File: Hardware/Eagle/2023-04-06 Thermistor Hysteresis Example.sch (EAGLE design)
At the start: 7 parts, among them U1 LMV339

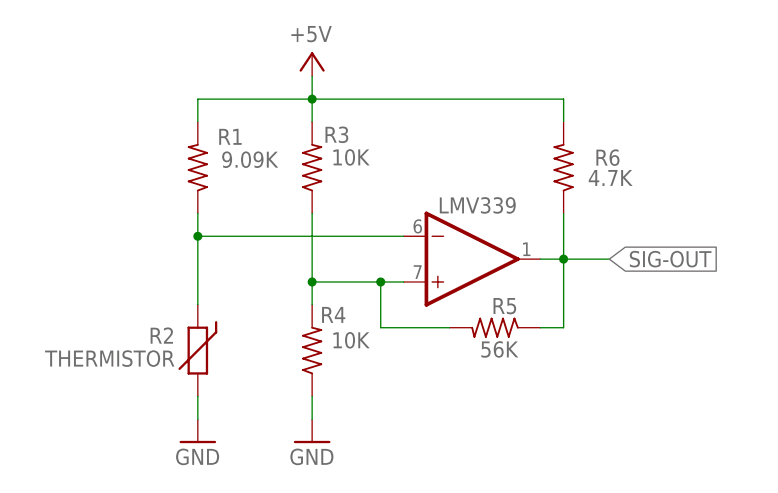
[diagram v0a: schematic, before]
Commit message: LN2 autofill update
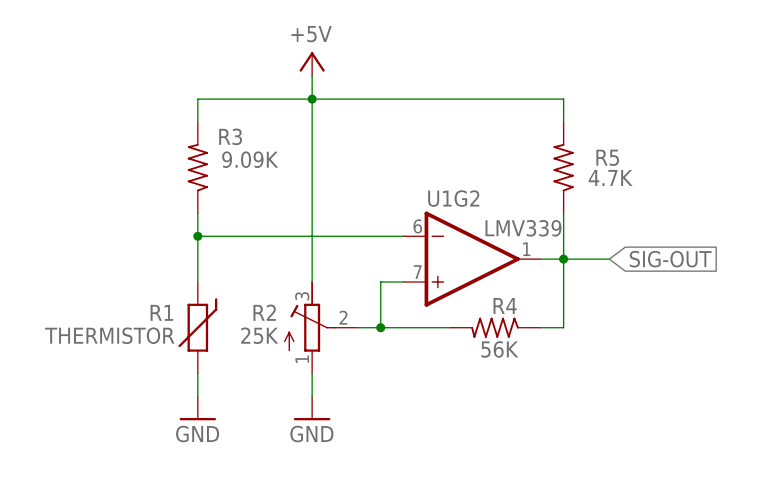
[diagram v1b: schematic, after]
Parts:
- removed R6: 4.7K, AUmlib:R-US_R0805
- R1: value 9.09K -> THERMISTOR; device AUmlib:R-US_R0805 -> varistor:THERMISTOR-7,5
- R2: value THERMISTOR -> 25K; device varistor:THERMISTOR-7,5 -> AUmlib:R-TRIMM3296Y
- R3: value 10K -> 9.09K
- R4: value 10K -> 56K
- R5: value 56K -> 4.7K
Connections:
- net +5V: now also R2.E, R5.2; no longer R1.2, R6.2
- net GND: now also R1.2, R2.A; no longer R2.2, R4.1
- net SIG-OUT: now also R4.1; no longer R6.1
- net THER3-IN: now also R3.1; no longer R2.1
- net TRIM3: now also R2.S; no longer R3.1, R5.2
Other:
- moved on the sheet: R3, R4, R5
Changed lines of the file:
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@@
 <?xml version="1.0" encoding="utf-8"?>
 <!DOCTYPE eagle SYSTEM "eagle.dtd">
-<eagle version="9.6.2">
+<eagle version="9.5.2">
 <drawing>
 <settings>
@@
 <setting verticaltext="up"/>
 </settings>
-<grid distance="0.05" unitdist="inch" unit="inch" style="lines" multiple="1" display="yes" altdistance="0.01" altunitdist="inch" altunit="inch"/>
+<grid distance="0.1" unitdist="inch" unit="inch" style="lines" multiple="1" display="yes" altdistance="0.01" altunitdist="inch" altunit="inch"/>
 <layers>
 <layer number="1" name="Top" color="4" fill="1" visible="no" active="no"/>
@@
 </classes>
 <parts>
-<part name="R6" library="AUmlib" library_urn="urn:adsk.eagle:library:9166017" deviceset="R-US_" device="R0805" package3d_urn="urn:adsk.eagle:package:4021199/4" value="4.7K"/>
+<part name="R5" library="AUmlib" library_urn="urn:adsk.eagle:library:9166017" deviceset="R-US_" device="R0805" package3d_urn="urn:adsk.eagle:package:4021199/1" value="4.7K"/>
 <part name="P+3" library="AUmlib" library_urn="urn:adsk.eagle:library:9166017" deviceset="+5V" device=""/>
-<part name="R5" library="AUmlib" library_urn="urn:adsk.eagle:library:9166017" deviceset="R-US_" device="R0805" package3d_urn="urn:adsk.eagle:package:4021199/4" value="56K"/>
-<part name="R1" library="AUmlib" library_urn="urn:adsk.eagle:library:9166017" deviceset="R-US_" device="R0805" package3d_urn="urn:adsk.eagle:package:4021199/4" value="9.09K"/>
+<part name="R4" library="AUmlib" library_urn="urn:adsk.eagle:library:9166017" deviceset="R-US_" device="R0805" package3d_urn="urn:adsk.eagle:package:4021199/1" value="56K"/>
+<part name="R3" library="AUmlib" library_urn="urn:adsk.eagle:library:9166017" deviceset="R-US_" device="R0805" package3d_urn="urn:adsk.eagle:package:4021199/1" value="9.09K"/>
+<part name="R2" library="AUmlib" library_urn="urn:adsk.eagle:library:9166017" deviceset="R-TRIMM" device="3296Y" package3d_urn="urn:adsk.eagle:package:16459115/2" value="25K"/>
 <part name="U1" library="AUmlib" library_urn="urn:adsk.eagle:library:9166017" deviceset="LM339" device="SOIC-14" package3d_urn="urn:adsk.eagle:package:3812082/2" value="LMV339"/>
-<part name="R2" library="varistor" library_urn="urn:adsk.eagle:library:410" deviceset="THERMISTOR" device="-7,5" package3d_urn="urn:adsk.eagle:package:30593/1" value="THERMISTOR"/>
+<part name="R1" library="varistor" library_urn="urn:adsk.eagle:library:410" deviceset="THERMISTOR" device="-7,5" package3d_urn="urn:adsk.eagle:package:30593/1" value="THERMISTOR"/>
 <part name="GND1" library="AUmlib" library_urn="urn:adsk.eagle:library:9166017" deviceset="GND" device=""/>
 <part name="GND2" library="AUmlib" library_urn="urn:adsk.eagle:library:9166017" deviceset="GND" device=""/>
-<part name="R3" library="AUmlib" library_urn="urn:adsk.eagle:library:9166017" deviceset="R-US_" device="R0805" package3d_urn="urn:adsk.eagle:package:4021199/4" value="10K"/>
-<part name="R4" library="AUmlib" library_urn="urn:adsk.eagle:library:9166017" deviceset="R-US_" device="R0805" package3d_urn="urn:adsk.eagle:package:4021199/4" value="10K"/>
 </parts>
 <sheets>
@@
 </plain>
 <instances>
-<instance part="R6" gate="G$1" x="50.8" y="35.56" smashed="yes" rot="MR90">
+<instance part="R5" gate="G$1" x="50.8" y="35.56" smashed="yes" rot="MR90">
 <attribute name="NAME" x="57.15" y="35.7886" size="1.778" layer="95" rot="MR0"/>
 <attribute name="VALUE" x="58.42" y="33.528" size="1.778" layer="96" rot="MR0"/>
@@
 <attribute name="VALUE" x="20.32" y="49.53" size="1.778" layer="96" rot="MR0" align="bottom-right"/>
 </instance>
-<instance part="R5" gate="G$1" x="43.18" y="17.78" smashed="yes" rot="MR0">
+<instance part="R4" gate="G$1" x="43.18" y="17.78" smashed="yes" rot="MR0">
 <attribute name="NAME" x="45.72" y="19.304" size="1.778" layer="95" rot="MR0"/>
 <attribute name="VALUE" x="45.72" y="14.478" size="1.778" layer="96" rot="MR0"/>
 </instance>
-<instance part="R1" gate="G$1" x="10.16" y="35.56" smashed="yes" rot="MR90">
+<instance part="R3" gate="G$1" x="10.16" y="35.56" smashed="yes" rot="MR90">
 <attribute name="NAME" x="15.24" y="38.1" size="1.778" layer="95" rot="MR0"/>
 <attribute name="VALUE" x="19.05" y="35.56" size="1.778" layer="96" rot="MR0"/>
 </instance>
+<instance part="R2" gate="G$1" x="22.86" y="17.78" smashed="yes">
+<attribute name="NAME" x="19.05" y="20.32" size="1.778" layer="95" rot="R180"/>
+<attribute name="VALUE" x="19.05" y="17.78" size="1.778" layer="96" rot="R180"/>
+</instance>
 <instance part="U1" gate="G2" x="40.64" y="25.4" smashed="yes">
-<attribute name="VALUE" x="36.83" y="30.48" size="1.778" layer="95"/>
-</instance>
-<instance part="R2" gate="G$1" x="10.16" y="15.24" smashed="yes" rot="R90">
-<attribute name="NAME" x="7.62" y="17.78" size="1.778" layer="95" rot="R180"/>
-<attribute name="VALUE" x="7.62" y="15.24" size="1.778" layer="96" rot="R180"/>
-</instance>
-<instance part="GND1" gate="1" x="22.86" y="5.08" smashed="yes">
-<attribute name="VALUE" x="20.32" y="2.54" size="1.778" layer="96"/>
-</instance>
-<instance part="GND2" gate="1" x="10.16" y="5.08" smashed="yes">
-<attribute name="VALUE" x="7.62" y="2.54" size="1.778" layer="96"/>
-</instance>
-<instance part="R3" gate="G$1" x="22.86" y="35.56" smashed="yes" rot="R90">
-<attribute name="NAME" x="24.13" y="38.3286" size="1.778" layer="95"/>
-<attribute name="VALUE" x="29.21" y="37.592" size="1.778" layer="96" rot="R180"/>
-</instance>
-<instance part="R4" gate="G$1" x="22.86" y="15.24" smashed="yes" rot="R90">
-<attribute name="NAME" x="26.67" y="20.0914" size="1.778" layer="95" rot="R180"/>
-<attribute name="VALUE" x="29.21" y="17.272" size="1.778" layer="96" rot="R180"/>
+<attribute name="NAME" x="35.56" y="31.242" size="1.778" layer="95"/>
+<attribute name="VALUE" x="41.91" y="27.94" size="1.778" layer="95"/>
+</instance>
+<instance part="R1" gate="G$1" x="10.16" y="17.78" smashed="yes" rot="R90">
+<attribute name="NAME" x="7.62" y="20.32" size="1.778" layer="95" rot="R180"/>
+<attribute name="VALUE" x="7.62" y="17.78" size="1.778" layer="96" rot="R180"/>
+</instance>
+<instance part="GND1" gate="1" x="22.86" y="7.62" smashed="yes">
+<attribute name="VALUE" x="20.32" y="5.08" size="1.778" layer="96"/>
+</instance>
+<instance part="GND2" gate="1" x="10.16" y="7.62" smashed="yes">
+<attribute name="VALUE" x="7.62" y="5.08" size="1.778" layer="96"/>
 </instance>
 </instances>
@@
 <net name="SIG-OUT" class="0">
 <segment>
-<pinref part="R6" gate="G$1" pin="1"/>
+<pinref part="R5" gate="G$1" pin="1"/>
 <wire x1="50.8" y1="30.48" x2="50.8" y2="25.4" width="0.1524" layer="91"/>
-<pinref part="R5" gate="G$1" pin="1"/>
+<pinref part="R4" gate="G$1" pin="1"/>
 <wire x1="48.26" y1="17.78" x2="50.8" y2="17.78" width="0.1524" layer="91"/>
 <wire x1="50.8" y1="17.78" x2="50.8" y2="25.4" width="0.1524" layer="91"/>
@@
 <net name="TRIM3" class="0">
 <segment>
-<pinref part="R5" gate="G$1" pin="2"/>
+<pinref part="R4" gate="G$1" pin="2"/>
 <wire x1="38.1" y1="17.78" x2="30.48" y2="17.78" width="0.1524" layer="91"/>
 <wire x1="30.48" y1="17.78" x2="30.48" y2="22.86" width="0.1524" layer="91"/>
+<wire x1="30.48" y1="17.78" x2="27.94" y2="17.78" width="0.1524" layer="91"/>
+<junction x="30.48" y="17.78"/>
+<pinref part="R2" gate="G$1" pin="S"/>
 <pinref part="U1" gate="G2" pin="+IN"/>
 <wire x1="33.02" y1="22.86" x2="30.48" y2="22.86" width="0.1524" layer="91"/>
+</segment>
+</net>
+<net name="THER3-IN" class="0">
+<segment>
 <pinref part="R3" gate="G$1" pin="1"/>
-<pinref part="R4" gate="G$1" pin="2"/>
-<wire x1="22.86" y1="30.48" x2="22.86" y2="22.86" width="0.1524" layer="91"/>
-<wire x1="22.86" y1="22.86" x2="22.86" y2="20.32" width="0.1524" layer="91"/>
-<wire x1="22.86" y1="22.86" x2="30.48" y2="22.86" width="0.1524" layer="91"/>
-<junction x="22.86" y="22.86"/>
-<junction x="30.48" y="22.86"/>
-</segment>
-</net>
-<net name="THER3-IN" class="0">
-<segment>
 <pinref part="R1" gate="G$1" pin="1"/>
-<pinref part="R2" gate="G$1" pin="1"/>
-<wire x1="10.16" y1="20.32" x2="10.16" y2="27.94" width="0.1524" layer="91"/>
+<wire x1="10.16" y1="22.86" x2="10.16" y2="27.94" width="0.1524" layer="91"/>
 <pinref part="U1" gate="G2" pin="-IN"/>
 <wire x1="10.16" y1="27.94" x2="10.16" y2="30.48" width="0.1524" layer="91"/>
@@
 <net name="GND" class="0">
 <segment>
+<pinref part="R2" gate="G$1" pin="A"/>
 <pinref part="GND1" gate="1" pin="GND"/>
-<wire x1="22.86" y1="7.62" x2="22.86" y2="10.16" width="0.1524" layer="91"/>
-<pinref part="R4" gate="G$1" pin="1"/>
+<wire x1="22.86" y1="10.16" x2="22.86" y2="12.7" width="0.1524" layer="91"/>
 </segment>
 <segment>
 <pinref part="GND2" gate="1" pin="GND"/>
-<pinref part="R2" gate="G$1" pin="2"/>
-<wire x1="10.16" y1="7.62" x2="10.16" y2="10.16" width="0.1524" layer="91"/>
+<pinref part="R1" gate="G$1" pin="2"/>
+<wire x1="10.16" y1="10.16" x2="10.16" y2="12.7" width="0.1524" layer="91"/>
 </segment>
 </net>
 <net name="+5V" class="0">
 <segment>
-<pinref part="R6" gate="G$1" pin="2"/>
+<pinref part="R5" gate="G$1" pin="2"/>
 <wire x1="50.8" y1="40.64" x2="50.8" y2="43.18" width="0.1524" layer="91"/>
 <wire x1="50.8" y1="43.18" x2="22.86" y2="43.18" width="0.1524" layer="91"/>
 <wire x1="10.16" y1="43.18" x2="22.86" y2="43.18" width="0.1524" layer="91"/>
+<wire x1="22.86" y1="43.18" x2="22.86" y2="22.86" width="0.1524" layer="91"/>
+<pinref part="R2" gate="G$1" pin="E"/>
 <pinref part="P+3" gate="1" pin="+5V"/>
 <wire x1="22.86" y1="43.18" x2="22.86" y2="45.72" width="0.1524" layer="91"/>
 <junction x="22.86" y="43.18"/>
-<pinref part="R1" gate="G$1" pin="2"/>
+<pinref part="R3" gate="G$1" pin="2"/>
 <wire x1="10.16" y1="40.64" x2="10.16" y2="43.18" width="0.1524" layer="91"/>
-<pinref part="R3" gate="G$1" pin="2"/>
-<wire x1="22.86" y1="40.64" x2="22.86" y2="43.18" width="0.1524" layer="91"/>
-</segment>
-</net>
+</segment>
+</net>
